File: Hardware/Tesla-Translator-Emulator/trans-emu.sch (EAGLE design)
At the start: 29 parts, among them U1 STM32F413RGT6, U2 TJA1042HVSON, U3 TJA1042HVSON, U4 TJA1042HVSON, Y1 CRYSTAL-3.2X2.54-PIN

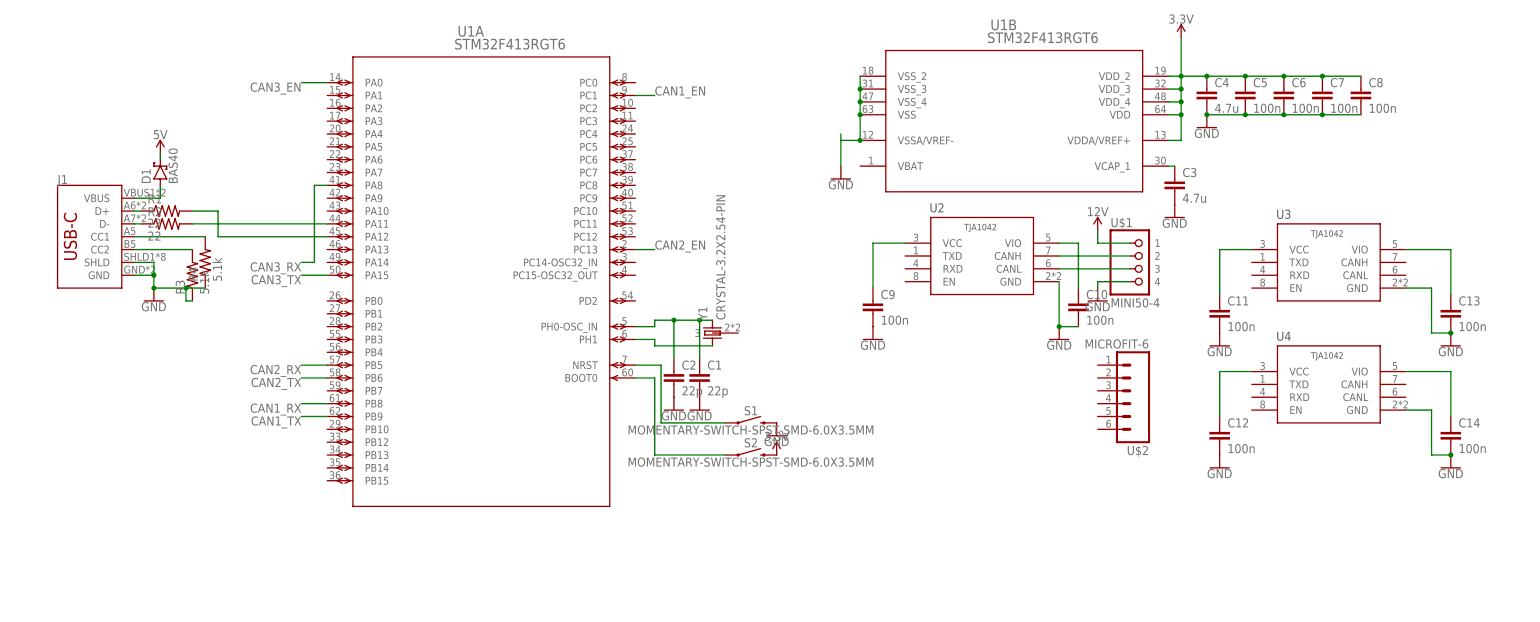
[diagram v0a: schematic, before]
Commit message: schematic complete board start ranlator emulator
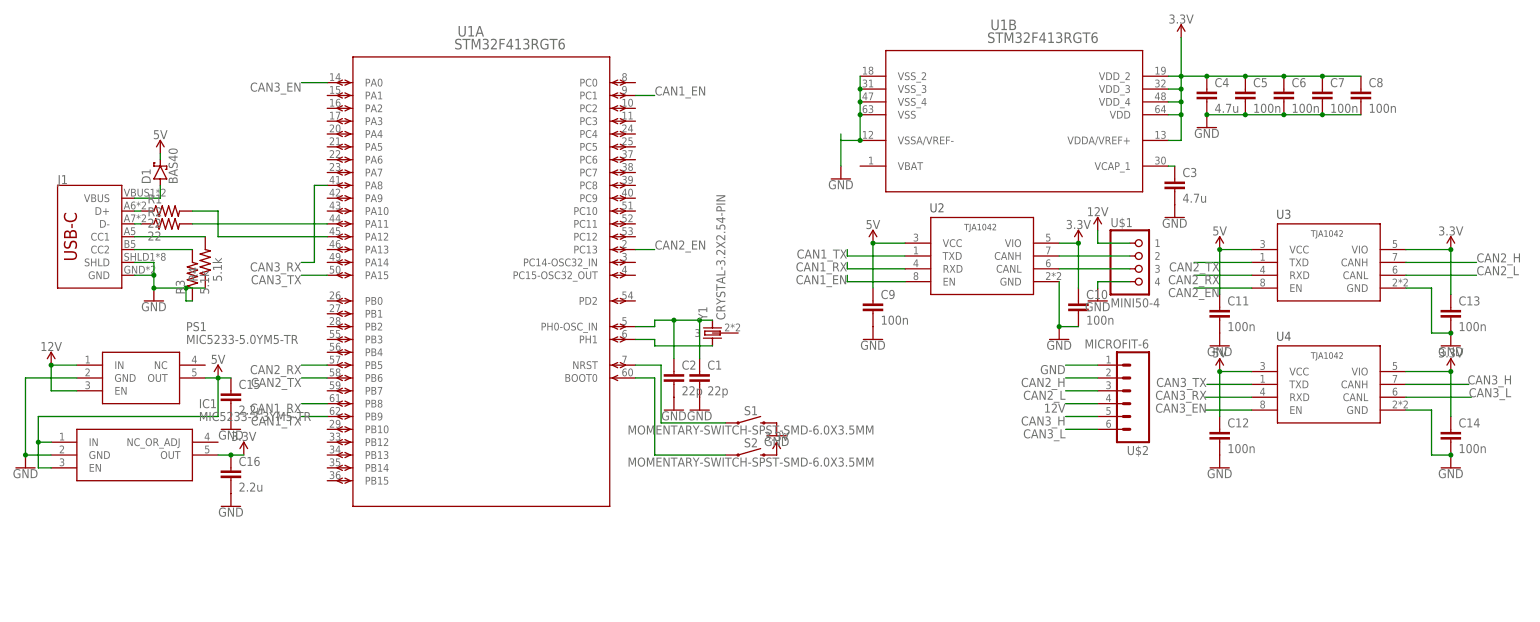
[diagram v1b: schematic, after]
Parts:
- added C15, C16: 2.2u, comma.ai:C0603
- added IC1: MIC5233-3.3YM5-TR, SamacSys_Parts:MIC5233-3.3YM5-TR
- added PS1: MIC5233-5.0YM5-TR, SamacSys_Parts:MIC5233-5.0YM5-TR
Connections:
- removed net N$17: C9.1, U2.VCC
- removed net N$18: C10.1, U2.VIO
- removed net N$19: C11.1, U3.VCC
- removed net N$20: C13.1, U3.VIO
- removed net N$21: C12.1, U4.VCC
- removed net N$22: C14.1, U4.VIO
- new net CAN2_H: U$2.2, U3.CANH
- new net CAN2_L: U$2.3, U3.CANL
- new net CAN3_H: U$2.5, U4.CANH
- new net CAN3_L: U$2.6, U4.CANL
- net 12V: now also PS1.EN, PS1.IN, U$2.4
- net 3.3V: now also C10.1, C13.1, C14.1, C16.1, IC1.OUT, U2.VIO, U3.VIO, U4.VIO
- net 5V: now also C11.1, C12.1, C15.1, C9.1, IC1.EN, IC1.IN, PS1.OUT, U2.VCC, U3.VCC, U4.VCC
- net CAN1_EN: now also U2.EN
- net CAN1_RX: now also U2.RXD
- net CAN1_TX: now also U2.TXD
- net CAN2_EN: now also U3.EN
- net CAN2_RX: now also U3.RXD
- net CAN2_TX: now also U3.TXD
- net CAN3_EN: now also U4.EN
- net CAN3_RX: now also U4.RXD
- net CAN3_TX: now also U4.TXD
- net GND: now also C15.2, C16.2, IC1.GND, PS1.GND, U$2.1

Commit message: boards
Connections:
- net N$1: no longer C2.1
- net N$2: now also C2.1
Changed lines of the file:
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@@
 <pinref part="Y1" gate="G$1" pin="2"/>
 <wire x1="107.95" y1="36.83" x2="105.41" y2="36.83" width="0.1524" layer="91"/>
-<pinref part="C2" gate="G$1" pin="1"/>
-<wire x1="105.41" y1="36.83" x2="100.33" y2="36.83" width="0.1524" layer="91"/>
-<wire x1="100.33" y1="36.83" x2="96.52" y2="36.83" width="0.1524" layer="91"/>
-<wire x1="100.33" y1="29.21" x2="100.33" y2="36.83" width="0.1524" layer="91"/>
-<junction x="100.33" y="36.83"/>
+<wire x1="105.41" y1="36.83" x2="96.52" y2="36.83" width="0.1524" layer="91"/>
 <pinref part="C1" gate="G$1" pin="1"/>
 <wire x1="105.41" y1="29.21" x2="105.41" y2="36.83" width="0.1524" layer="91"/>
 <junction x="105.41" y="36.83"/>
-</segment>
-</net>
-<net name="N$2" class="0">
-<segment>
-<pinref part="U1" gate="A" pin="PH1"/>
-<wire x1="92.71" y1="33.02" x2="96.52" y2="33.02" width="0.1524" layer="91"/>
-<wire x1="96.52" y1="33.02" x2="96.52" y2="31.75" width="0.1524" layer="91"/>
-<pinref part="Y1" gate="G$1" pin="1"/>
-<wire x1="107.95" y1="31.75" x2="96.52" y2="31.75" width="0.1524" layer="91"/>
 </segment>
 </net>
@@
 </segment>
 </net>
+<net name="N$2" class="0">
+<segment>
+<pinref part="C2" gate="G$1" pin="1"/>
+<wire x1="100.33" y1="29.21" x2="100.33" y2="31.75" width="0.1524" layer="91"/>
+<pinref part="Y1" gate="G$1" pin="1"/>
+<wire x1="107.95" y1="31.75" x2="100.33" y2="31.75" width="0.1524" layer="91"/>
+<junction x="100.33" y="31.75"/>
+<wire x1="100.33" y1="31.75" x2="96.52" y2="31.75" width="0.1524" layer="91"/>
+<wire x1="96.52" y1="33.02" x2="96.52" y2="31.75" width="0.1524" layer="91"/>
+<pinref part="U1" gate="A" pin="PH1"/>
+<wire x1="92.71" y1="33.02" x2="96.52" y2="33.02" width="0.1524" layer="91"/>
+</segment>
+</net>

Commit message: final board prep for manufacture
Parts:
- added R5, R6: 120, comma.ai:R0402
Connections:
- net CAN2_H: now also R5.1
- net CAN2_L: now also R5.2
- net CAN3_H: now also R6.1
- net CAN3_L: now also R6.2
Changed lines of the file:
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@@
 <part name="GND17" library="SparkFun-PowerSymbols" library_urn="urn:adsk.eagle:library:530" deviceset="GND" device=""/>
 <part name="SUPPLY13" library="SparkFun-PowerSymbols" library_urn="urn:adsk.eagle:library:530" deviceset="3.3V" device=""/>
+<part name="R5" library="comma.ai" deviceset="R" device="0402" value="120"/>
+<part name="R6" library="comma.ai" deviceset="R" device="0402" value="120"/>
 </parts>
 <sheets>
@@
 <instance part="SUPPLY13" gate="G$1" x="180.34" y="52.07" smashed="yes">
 <attribute name="VALUE" x="180.34" y="54.864" size="1.778" layer="96" align="bottom-center"/>
+</instance>
+<instance part="R5" gate="G$1" x="162.56" y="25.4" smashed="yes" rot="R180">
+<attribute name="NAME" x="166.37" y="23.9014" size="1.778" layer="95" rot="R180"/>
+<attribute name="VALUE" x="166.37" y="28.702" size="1.778" layer="96" rot="R180"/>
+</instance>
+<instance part="R6" gate="G$1" x="162.56" y="17.78" smashed="yes" rot="R180">
+<attribute name="NAME" x="166.37" y="16.2814" size="1.778" layer="95" rot="R180"/>
+<attribute name="VALUE" x="166.37" y="21.082" size="1.778" layer="96" rot="R180"/>
 </instance>
 </instances>
@@
 <segment>
 <pinref part="U$2" gate="G$1" pin="2"/>
-<wire x1="184.15" y1="25.4" x2="177.8" y2="25.4" width="0.1524" layer="91"/>
 <label x="177.8" y="25.4" size="1.778" layer="95" rot="R180"/>
+<pinref part="R5" gate="G$1" pin="1"/>
+<wire x1="167.64" y1="25.4" x2="184.15" y2="25.4" width="0.1524" layer="91"/>
 </segment>
 </net>
@@
 <segment>
 <pinref part="U$2" gate="G$1" pin="3"/>
-<wire x1="184.15" y1="22.86" x2="177.8" y2="22.86" width="0.1524" layer="91"/>
 <label x="177.8" y="22.86" size="1.778" layer="95" rot="R180"/>
+<wire x1="184.15" y1="22.86" x2="157.48" y2="22.86" width="0.1524" layer="91"/>
+<pinref part="R5" gate="G$1" pin="2"/>
+<wire x1="157.48" y1="22.86" x2="157.48" y2="25.4" width="0.1524" layer="91"/>
 </segment>
 </net>
@@
 <segment>
 <pinref part="U$2" gate="G$1" pin="5"/>
-<wire x1="184.15" y1="17.78" x2="177.8" y2="17.78" width="0.1524" layer="91"/>
 <label x="177.8" y="17.78" size="1.778" layer="95" rot="R180"/>
+<pinref part="R6" gate="G$1" pin="1"/>
+<wire x1="167.64" y1="17.78" x2="184.15" y2="17.78" width="0.1524" layer="91"/>
 </segment>
 </net>
@@
 <segment>
 <pinref part="U$2" gate="G$1" pin="6"/>
-<wire x1="184.15" y1="15.24" x2="177.8" y2="15.24" width="0.1524" layer="91"/>
 <label x="177.8" y="15.24" size="1.778" layer="95" rot="R180"/>
-</segment>
-</net>
+<pinref part="R6" gate="G$1" pin="2"/>
+<wire x1="157.48" y1="17.78" x2="157.48" y2="15.24" width="0.1524" layer="91"/>
+<wire x1="157.48" y1="15.24" x2="184.15" y2="15.24" width="0.1524" layer="91"/>
+</segment>
+</net>

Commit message: signal switching
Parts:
- added Q1: PMOSFET, Transistor:PMOSFET_SOT23
- added Q2: NMOSFET, Transistor:NMOSFETSOT23
- added R7, R8: 10k, comma.ai:R0402
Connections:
- new net N$15: Q1.D, U$2.4
- new net N$16: Q1.G, Q2.D, R7.1
- new net PWRON: Q2.G, R8.2, U1A.PB12
- net 12V: now also Q1.S, R7.2; no longer U$2.4
- net GND: now also Q2.S, R8.1
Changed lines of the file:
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@@
 <part name="R5" library="comma.ai" deviceset="R" device="0402" value="120"/>
 <part name="R6" library="comma.ai" deviceset="R" device="0402" value="120"/>
+<part name="Q1" library="Transistor" library_urn="urn:adsk.eagle:library:16378713" deviceset="PMOSFET" device="SOT23" package3d_urn="urn:adsk.eagle:package:28738/2" technology="_" value="PMOSFET"/>
+<part name="R7" library="comma.ai" deviceset="R" device="0402" value="10k"/>
+<part name="Q2" library="Transistor" library_urn="urn:adsk.eagle:library:16378713" deviceset="NMOSFET" device="SOT23" package3d_urn="urn:adsk.eagle:package:28738/2" value="NMOSFET"/>
+<part name="R8" library="comma.ai" deviceset="R" device="0402" value="10k"/>
+<part name="GND18" library="SparkFun-PowerSymbols" library_urn="urn:adsk.eagle:library:530" deviceset="GND" device=""/>
 </parts>
 <sheets>
@@
 <attribute name="NAME" x="166.37" y="16.2814" size="1.778" layer="95" rot="R180"/>
 <attribute name="VALUE" x="166.37" y="21.082" size="1.778" layer="96" rot="R180"/>
+</instance>
+<instance part="Q1" gate="G$1" x="149.86" y="17.78" smashed="yes" rot="R90">
+<attribute name="NAME" x="148.59" y="24.13" size="1.778" layer="95" rot="R90"/>
+<attribute name="VALUE" x="151.13" y="24.13" size="1.778" layer="96" rot="R90"/>
+</instance>
+<instance part="R7" gate="G$1" x="142.24" y="15.24" smashed="yes" rot="R90">
+<attribute name="NAME" x="140.7414" y="11.43" size="1.778" layer="95" rot="R90"/>
+<attribute name="VALUE" x="145.542" y="11.43" size="1.778" layer="96" rot="R90"/>
+</instance>
+<instance part="Q2" gate="G$1" x="144.78" y="0" smashed="yes">
+<attribute name="NAME" x="151.13" y="1.27" size="1.778" layer="95"/>
+<attribute name="VALUE" x="151.13" y="-1.27" size="1.778" layer="96"/>
+</instance>
+<instance part="R8" gate="G$1" x="139.7" y="-7.62" smashed="yes" rot="R90">
+<attribute name="NAME" x="138.2014" y="-11.43" size="1.778" layer="95" rot="R90"/>
+<attribute name="VALUE" x="143.002" y="-11.43" size="1.778" layer="96" rot="R90"/>
+</instance>
+<instance part="GND18" gate="1" x="144.78" y="-17.78" smashed="yes">
+<attribute name="VALUE" x="144.78" y="-18.034" size="1.778" layer="96" align="top-center"/>
 </instance>
 </instances>
@@
 <pinref part="C15" gate="G$1" pin="2"/>
 <pinref part="GND17" gate="1" pin="GND"/>
+</segment>
+<segment>
+<pinref part="Q2" gate="G$1" pin="S"/>
+<wire x1="147.32" y1="-5.08" x2="147.32" y2="-15.24" width="0.1524" layer="91"/>
+<pinref part="R8" gate="G$1" pin="1"/>
+<wire x1="147.32" y1="-15.24" x2="144.78" y2="-15.24" width="0.1524" layer="91"/>
+<wire x1="144.78" y1="-15.24" x2="139.7" y2="-15.24" width="0.1524" layer="91"/>
+<wire x1="139.7" y1="-15.24" x2="139.7" y2="-12.7" width="0.1524" layer="91"/>
+<pinref part="GND18" gate="1" pin="GND"/>
+<junction x="144.78" y="-15.24"/>
 </segment>
 </net>
@@
 </segment>
 <segment>
-<pinref part="U$2" gate="G$1" pin="4"/>
-<wire x1="184.15" y1="20.32" x2="177.8" y2="20.32" width="0.1524" layer="91"/>
-<label x="177.8" y="20.32" size="1.778" layer="95" rot="R180"/>
-</segment>
-<segment>
 <pinref part="PS1" gate="G$1" pin="EN"/>
 <wire x1="-17.78" y1="22.86" x2="-22.86" y2="22.86" width="0.1524" layer="91"/>
@@
 <pinref part="SUPPLY6" gate="G$1" pin="12V"/>
 <junction x="-22.86" y="27.94"/>
+</segment>
+<segment>
+<pinref part="Q1" gate="G$1" pin="S"/>
+<wire x1="144.78" y1="20.32" x2="142.24" y2="20.32" width="0.1524" layer="91"/>
+<label x="137.16" y="20.32" size="1.778" layer="95"/>
+<pinref part="R7" gate="G$1" pin="2"/>
+<wire x1="142.24" y1="20.32" x2="137.16" y2="20.32" width="0.1524" layer="91"/>
+<junction x="142.24" y="20.32"/>
 </segment>
 </net>
@@
 </segment>
 </net>
+<net name="N$15" class="0">
+<segment>
+<pinref part="U$2" gate="G$1" pin="4"/>
+<pinref part="Q1" gate="G$1" pin="D"/>
+<wire x1="184.15" y1="20.32" x2="154.94" y2="20.32" width="0.1524" layer="91"/>
+</segment>
+</net>
+<net name="PWRON" class="0">
+<segment>
+<pinref part="U1" gate="A" pin="PB12"/>
+<wire x1="31.75" y1="12.7" x2="27.94" y2="12.7" width="0.1524" layer="91"/>
+<label x="27.94" y="12.7" size="1.778" layer="95" rot="R180"/>
+</segment>
+<segment>
+<pinref part="Q2" gate="G$1" pin="G"/>
+<pinref part="R8" gate="G$1" pin="2"/>
+<wire x1="142.24" y1="-2.54" x2="139.7" y2="-2.54" width="0.1524" layer="91"/>
+<label x="139.7" y="-2.54" size="1.778" layer="95" rot="R180"/>
+</segment>
+</net>
+<net name="N$16" class="0">
+<segment>
+<pinref part="Q1" gate="G$1" pin="G"/>
+<wire x1="147.32" y1="15.24" x2="147.32" y2="10.16" width="0.1524" layer="91"/>
+<pinref part="R7" gate="G$1" pin="1"/>
+<wire x1="147.32" y1="10.16" x2="147.32" y2="5.08" width="0.1524" layer="91"/>
+<wire x1="142.24" y1="10.16" x2="147.32" y2="10.16" width="0.1524" layer="91"/>
+<junction x="147.32" y="10.16"/>
+<pinref part="Q2" gate="G$1" pin="D"/>
+</segment>
+</net>
